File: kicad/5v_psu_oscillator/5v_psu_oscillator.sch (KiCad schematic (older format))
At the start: 30 parts, among them P1 IEC-C6, P2 CONN_01X03, SW1 DPST, T1 BV 030-7329.0 T, U1 LT1017, U2 74HC08, U3 LM2675N-5.0, U4 74HC4024

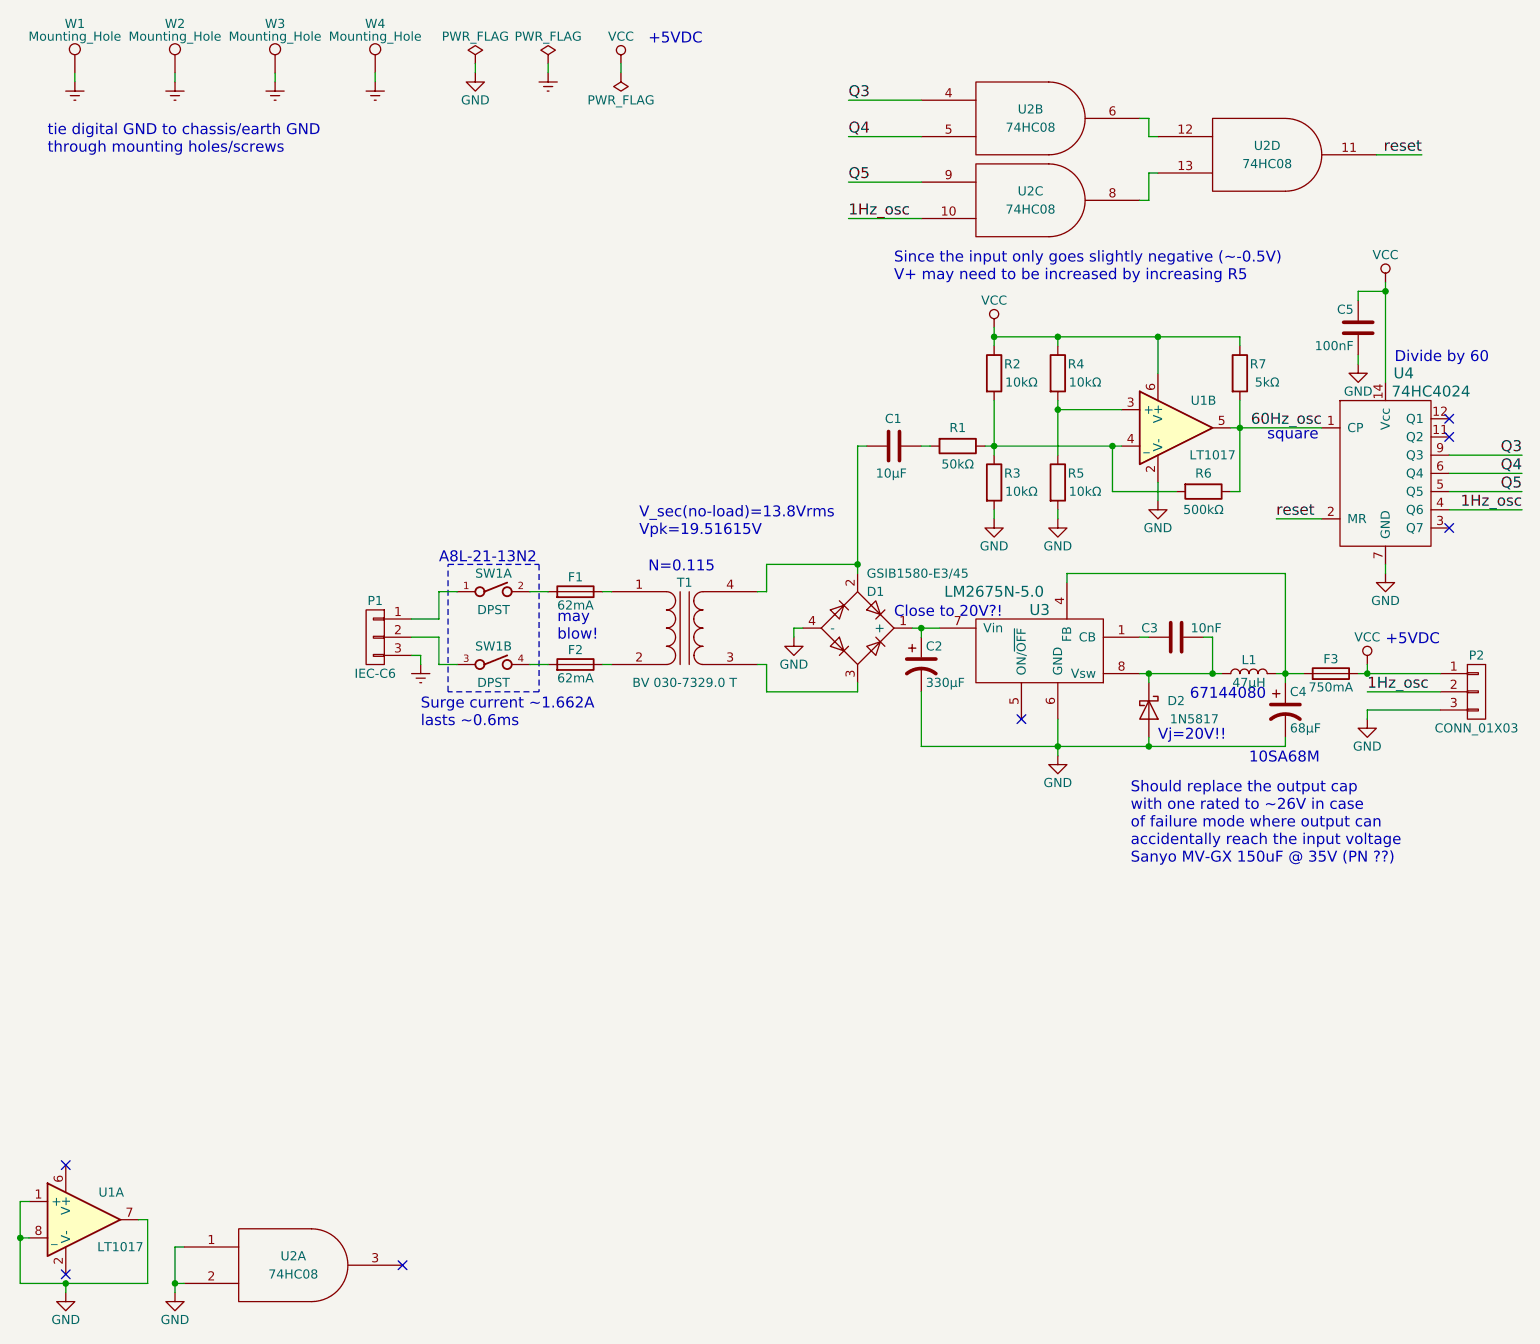
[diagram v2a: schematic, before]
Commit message: Add new 5V psu and oscillator simulation projects/data, include additional 100uFinput capacitor to the buck converter for less input ripple
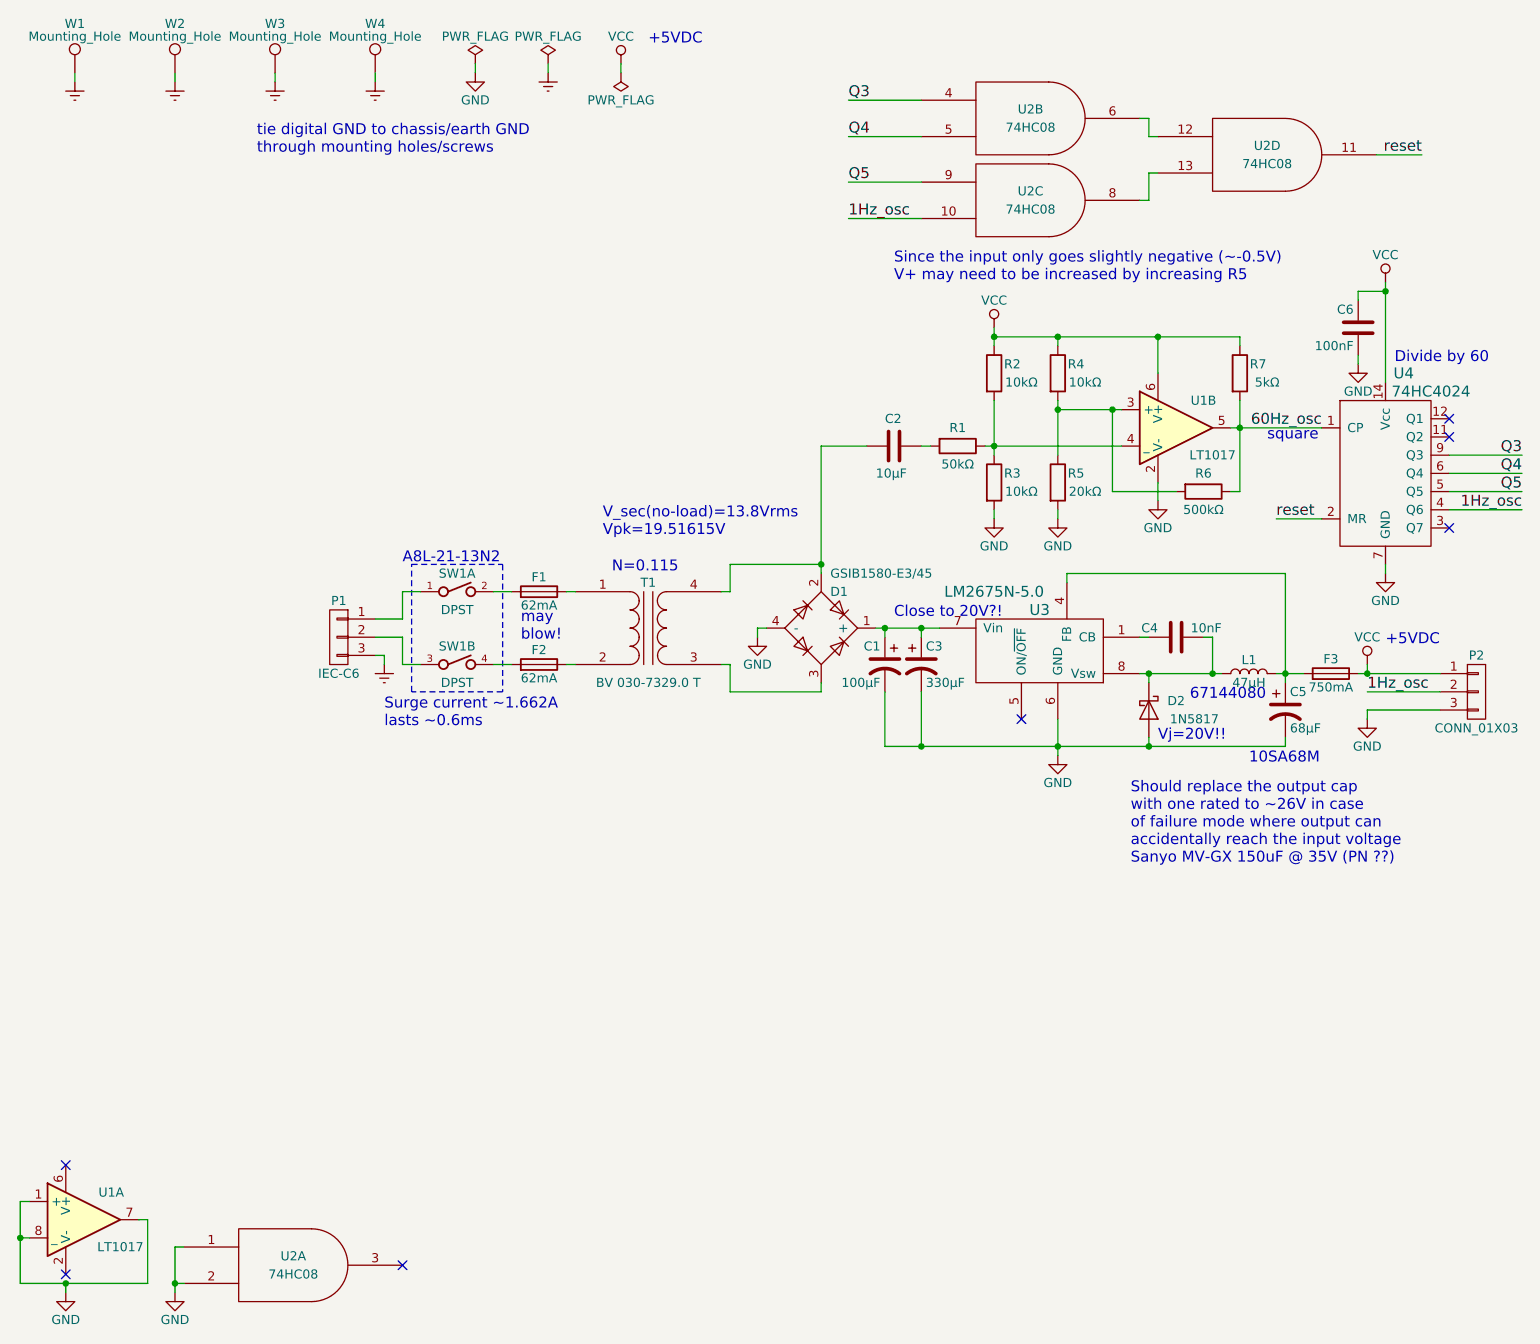
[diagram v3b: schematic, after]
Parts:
- added C1: 100μF, symbol CP1
- R5: value 10kΩ -> 20kΩ
- renumbered C1 to C2, C2 to C3, C3 to C4, C4 to C5, C5 to C6
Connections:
- net GND: now also C1.2
- net at C3.1, D1.1 (+), U3.7 (Vin): now also C1.1
- net at R1.1, R2.2, R3.1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: no longer R6.2
- net at R4.2, R5.1, U1.3 (+): now also R6.2
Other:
- moved on the sheet: D1, F1, F2, P1, SW1A, SW1B, T1
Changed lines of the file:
@@
 L Transformer_1P_1S T1
 U 1 1 59065B01
-P 4200 3900
-F 0 "T1" H 4200 4150 50  0000 C CNN
-F 1 "BV 030-7329.0 T" H 4200 3600 50  0000 C CNN
-F 2 "" H 4200 3900 50  0001 C CNN
-F 3 "" H 4200 3900 50  0000 C CNN
-	1    4200 3900
+P 4000 3900
+F 0 "T1" H 4000 4150 50  0000 C CNN
+F 1 "BV 030-7329.0 T" H 4000 3600 50  0000 C CNN
+F 2 "" H 4000 3900 50  0001 C CNN
+F 3 "" H 4000 3900 50  0000 C CNN
+	1    4000 3900
 	1    0    0    -1
 $EndComp
@@
 L Fuse F1
 U 1 1 59065C6E
-P 3600 3700
-F 0 "F1" V 3680 3700 50  0000 C CNN
-F 1 "62mA" V 3525 3700 50  0000 C CNN
-F 2 "Resistors_THT:R_Axial_DIN0309_L9.0mm_D3.2mm_P12.70mm_Horizontal" V 3530 3700 50  0001 C CNN
-F 3 "" H 3600 3700 50  0000 C CNN
-	1    3600 3700
+P 3400 3700
+F 0 "F1" V 3480 3700 50  0000 C CNN
+F 1 "62mA" V 3325 3700 50  0000 C CNN
+F 2 "Resistors_THT:R_Axial_DIN0309_L9.0mm_D3.2mm_P12.70mm_Horizontal" V 3330 3700 50  0001 C CNN
+F 3 "" H 3400 3700 50  0000 C CNN
+	1    3400 3700
 	0    1    -1   0
 $EndComp
@@
 L Fuse F2
 U 1 1 59065D5D
-P 3600 4100
-F 0 "F2" V 3680 4100 50  0000 C CNN
-F 1 "62mA" V 3525 4100 50  0000 C CNN
-F 2 "Resistors_THT:R_Axial_DIN0309_L9.0mm_D3.2mm_P12.70mm_Horizontal" V 3530 4100 50  0001 C CNN
-F 3 "" H 3600 4100 50  0000 C CNN
-	1    3600 4100
+P 3400 4100
+F 0 "F2" V 3480 4100 50  0000 C CNN
+F 1 "62mA" V 3325 4100 50  0000 C CNN
+F 2 "Resistors_THT:R_Axial_DIN0309_L9.0mm_D3.2mm_P12.70mm_Horizontal" V 3330 4100 50  0001 C CNN
+F 3 "" H 3400 4100 50  0000 C CNN
+	1    3400 4100
 	0    1    -1   0
 $EndComp
@@
 L D_Bridge_+AA- D1
 U 1 1 59065F83
-P 5150 3900
-F 0 "D1" H 5200 4100 50  0000 L CNN
-F 1 "GSIB1580-E3/45" H 5200 4200 50  0000 L CNN
-F 2 "" H 5150 3900 50  0001 C CNN
-F 3 "" H 5150 3900 50  0000 C CNN
-	1    5150 3900
+P 4950 3900
+F 0 "D1" H 5000 4100 50  0000 L CNN
+F 1 "GSIB1580-E3/45" H 5000 4200 50  0000 L CNN
+F 2 "" H 4950 3900 50  0001 C CNN
+F 3 "" H 4950 3900 50  0000 C CNN
+	1    4950 3900
 	1    0    0    -1
 $EndComp
@@
 L DPST SW1
 U 1 1 59066ED6
-P 3150 3700
-F 0 "SW1" H 3150 3800 50  0000 C CNN
-F 1 "DPST" H 3150 3600 50  0000 C CNN
-F 2 "" H 3150 3700 60  0001 C CNN
-F 3 "" H 3150 3700 60  0001 C CNN
-	1    3150 3700
+P 2950 3700
+F 0 "SW1" H 2950 3800 50  0000 C CNN
+F 1 "DPST" H 2950 3600 50  0000 C CNN
+F 2 "" H 2950 3700 60  0001 C CNN
+F 3 "" H 2950 3700 60  0001 C CNN
+	1    2950 3700
 	1    0    0    -1
 $EndComp
@@
 L DPST SW1
 U 2 1 59066F0F
-P 3150 4100
-F 0 "SW1" H 3150 4200 50  0000 C CNN
-F 1 "DPST" H 3150 4000 50  0000 C CNN
-F 2 "" H 3150 4100 60  0001 C CNN
-F 3 "" H 3150 4100 60  0001 C CNN
-	2    3150 4100
-	1    0    0    -1
-$EndComp
-$Comp
-L CP1 C2
+P 2950 4100
+F 0 "SW1" H 2950 4200 50  0000 C CNN
+F 1 "DPST" H 2950 4000 50  0000 C CNN
+F 2 "" H 2950 4100 60  0001 C CNN
+F 3 "" H 2950 4100 60  0001 C CNN
+	2    2950 4100
+	1    0    0    -1
+$EndComp
+$Comp
+L CP1 C3
 U 1 1 59067137
 P 5500 4100
-F 0 "C2" H 5525 4200 50  0000 L CNN
+F 0 "C3" H 5525 4200 50  0000 L CNN
 F 1 "330μF" H 5525 4000 50  0000 L CNN
 F 2 "Capacitors_THT:CP_Radial_D10.0mm_P5.00mm" H 5500 4100 50  0001 C CNN
@@
 	1    0    0    -1
 $EndComp
-Text Notes 3950 3400 0    60   ~ 0
+Text Notes 3750 3400 0    60   ~ 0
 V_sec(no-load)=13.8Vrms\nVpk=19.51615V
-Text Notes 4000 3600 0    60   ~ 0
+Text Notes 3800 3600 0    60   ~ 0
 N=0.115
 $Comp
@@
 $EndComp
 $Comp
-L C C3
+L C C4
 U 1 1 590696A4
 P 6900 3950
-F 0 "C3" V 6950 4050 50  0000 L CNN
+F 0 "C4" V 6950 4050 50  0000 L CNN
 F 1 "10nF" V 6950 3700 50  0000 L CNN
 F 2 "Capacitors_THT:C_Disc_D3.4mm_W2.1mm_P2.50mm" H 6938 3800 50  0001 C CNN
@@
 L CONN_01X03 P1
 U 1 1 5906AD4D
-P 2500 3950
-F 0 "P1" H 2500 4150 50  0000 C CNN
-F 1 "IEC-C6" H 2500 3750 50  0000 C CNN
-F 2 "" H 2500 3950 50  0001 C CNN
-F 3 "" H 2500 3950 50  0000 C CNN
-	1    2500 3950
+P 2300 3950
+F 0 "P1" H 2300 4150 50  0000 C CNN
+F 1 "IEC-C6" H 2300 3750 50  0000 C CNN
+F 2 "" H 2300 3950 50  0001 C CNN
+F 3 "" H 2300 3950 50  0000 C CNN
+	1    2300 3950
 	-1   0    0    -1
 $EndComp
@@
 $EndComp
 Wire Wire Line
-	4800 3950 4800 3900
-Wire Wire Line
-	4800 3900 4850 3900
-Wire Wire Line
-	4600 4100 4650 4100
-Wire Wire Line
-	4650 4100 4650 4250
-Wire Wire Line
-	5150 4250 5150 4200
-Wire Wire Line
-	4600 3700 4650 3700
-Wire Wire Line
-	4650 3700 4650 3550
-Wire Wire Line
-	4650 3550 5150 3550
-Wire Wire Line
-	5150 2900 5150 3600
-Wire Wire Line
-	3800 3700 3750 3700
-Wire Wire Line
-	3800 4100 3750 4100
-Wire Wire Line
-	3450 3700 3350 3700
-Wire Wire Line
-	3350 4100 3450 4100
-Wire Wire Line
-	2950 3700 2850 3700
-Wire Wire Line
-	2950 4100 2850 4100
+	4600 3950 4600 3900
+Wire Wire Line
+	4600 3900 4650 3900
+Wire Wire Line
+	4400 4100 4450 4100
+Wire Wire Line
+	4450 4100 4450 4250
+Wire Wire Line
+	4950 4250 4950 4200
+Wire Wire Line
+	4400 3700 4450 3700
+Wire Wire Line
+	4450 3700 4450 3550
+Wire Wire Line
+	4450 3550 4950 3550
+Wire Wire Line
+	4950 2900 4950 3600
+Wire Wire Line
+	3600 3700 3550 3700
+Wire Wire Line
+	3600 4100 3550 4100
+Wire Wire Line
+	3250 3700 3150 3700
+Wire Wire Line
+	3150 4100 3250 4100
+Wire Wire Line
+	2750 3700 2650 3700
+Wire Wire Line
+	2750 4100 2650 4100
 Wire Wire Line
 	5500 4550 5500 4250
 Wire Wire Line
-	5500 3950 5500 3900
-Wire Wire Line
-	5450 3900 5600 3900
+	5500 3900 5500 3950
+Wire Wire Line
+	5250 3900 5600 3900
 Connection ~ 5500 3900
 Wire Wire Line
 	6250 4400 6250 4600
 Wire Notes Line
-	2900 3550 3400 3550
+	2700 3550 3200 3550
 Wire Notes Line
-	3400 3550 3400 4250
+	3200 3550 3200 4250
 Wire Notes Line
-	3400 4250 2900 4250
+	3200 4250 2700 4250
 Wire Notes Line
-	2900 4250 2900 3550
+	2700 4250 2700 3550
 Wire Wire Line
 	6750 4550 6750 4500
@@
 	7950 4150 7950 4100
 Wire Wire Line
-	2750 4100 2750 4050
-Wire Wire Line
-	2750 4050 2700 4050
-Wire Wire Line
-	2700 3850 2850 3850
-Wire Wire Line
-	2850 3850 2850 3700
-Wire Wire Line
-	2700 3950 2850 3950
-Wire Wire Line
-	2850 3950 2850 4100
+	2550 4100 2550 4050
+Wire Wire Line
+	2550 4050 2500 4050
+Wire Wire Line
+	2500 3850 2650 3850
+Wire Wire Line
+	2650 3850 2650 3700
+Wire Wire Line
+	2500 3950 2650 3950
+Wire Wire Line
+	2650 3950 2650 4100
 Wire Wire Line
 	7950 4400 7950 4350
@@
 67144080
 $Comp
-L CP1 C4
+L CP1 C5
 U 1 1 59076BE1
 P 7500 4350
-F 0 "C4" H 7525 4450 50  0000 L CNN
+F 0 "C5" H 7525 4450 50  0000 L CNN
 F 1 "68μF" H 7525 4250 50  0000 L CNN
 F 2 "Capacitors_THT:CP_Radial_D6.3mm_P2.50mm" H 7500 4350 50  0001 C CNN
@@
 	1    0    0    -1
 $EndComp
-Text Notes 2850 3550 0    60   ~ 0
+Text Notes 2650 3550 0    60   ~ 0
 A8L-21-13N2
 NoConn ~ 6050 4400
-Text Notes 2750 4450 0    60   ~ 0
+Text Notes 2550 4450 0    60   ~ 0
 Surge current ~~1.662A\nlasts ~~0.6ms
 $Bitmap
@@
 Text Notes 5350 3850 0    60   ~ 0
 Close to 20V?!
-Text Notes 3500 3975 0    60   ~ 0
+Text Notes 3300 3975 0    60   ~ 0
 may\nblow!
 $Comp
@@
 P 6250 3100
 F 0 "R5" H 6350 3150 50  0000 C CNN
-F 1 "10kΩ" H 6400 3050 50  0000 C CNN
+F 1 "20kΩ" H 6400 3050 50  0000 C CNN
 F 2 "Resistors_THT:R_Axial_DIN0207_L6.3mm_D2.5mm_P7.62mm_Horizontal" V 6180 3100 50  0001 C CNN
 F 3 "" H 6250 3100 50  0000 C CNN
@@
 	6250 2650 6250 2950
 Wire Wire Line
-	6600 2700 6250 2700
+	6250 2700 6600 2700
 Connection ~ 6250 2700
 Connection ~ 5900 2900
@@
 $EndComp
 $Comp
-L C C1
+L C C2
 U 1 1 5908DC57
 P 5350 2900
-F 0 "C1" V 5200 2850 50  0000 L CNN
+F 0 "C2" V 5200 2850 50  0000 L CNN
 F 1 "10μF" V 5500 2800 50  0000 L CNN
 F 2 "Capacitors_THT:C_Disc_D5.0mm_W2.5mm_P2.50mm" H 5388 2750 50  0001 C CNN
@@
 	6900 3150 6550 3150
 Wire Wire Line
-	6550 3150 6550 2900
-Connection ~ 6550 2900
-Wire Wire Line
 	7250 3150 7200 3150
 Wire Wire Line
-	5150 2900 5200 2900
-Connection ~ 5150 3550
+	4950 2900 5200 2900
+Connection ~ 4950 3550
 Text Notes 7400 2875 0    60   ~ 0
 square
@@
 	5100 1650 5500 1650
 $Comp
-L C C5
+L C C6
 U 1 1 590A5FBC
 P 7900 2250
-F 0 "C5" H 7925 2350 50  0000 L CNN
+F 0 "C6" H 7925 2350 50  0000 L CNN
 F 1 "100nF" H 7925 2150 50  0000 L CNN
 F 2 "Capacitors_THT:C_Disc_D3.8mm_W2.6mm_P2.50mm" H 7938 2100 50  0001 C CNN
@@
 	6800 3100 6800 3200
 Wire Wire Line
-	4650 4250 5150 4250
-Wire Wire Line
-	5500 4550 7500 4550
+	4450 4250 4950 4250
+Wire Wire Line
+	5300 4550 7500 4550
 $Comp
 L GND #PWR01
 U 1 1 590B43E1
-P 4800 3950
-F 0 "#PWR01" H 4800 3700 50  0001 C CNN
-F 1 "GND" H 4800 3800 50  0000 C CNN
-F 2 "" H 4800 3950 50  0000 C CNN
-F 3 "" H 4800 3950 50  0000 C CNN
-	1    4800 3950
+P 4600 3950
+F 0 "#PWR01" H 4600 3700 50  0001 C CNN
+F 1 "GND" H 4600 3800 50  0000 C CNN
+F 2 "" H 4600 3950 50  0000 C CNN
+F 3 "" H 4600 3950 50  0000 C CNN
+	1    4600 3950
 	1    0    0    -1
 $EndComp
@@
 $EndComp
 NoConn ~ 800  6850
-Text Notes 700  1300 0    60   ~ 0
+Text Notes 1850 1300 0    60   ~ 0
 tie digital GND to chassis/earth GND\nthrough mounting holes/screws
 $Comp
@@
 L Earth #PWR018
 U 1 1 59DF4591
-P 2750 4100
-F 0 "#PWR018" H 2750 3850 50  0001 C CNN
-F 1 "Earth" H 2750 3950 50  0001 C CNN
-F 2 "" H 2750 4100 50  0001 C CNN
-F 3 "" H 2750 4100 50  0001 C CNN
-	1    2750 4100
+P 2550 4100
+F 0 "#PWR018" H 2550 3850 50  0001 C CNN
+F 1 "Earth" H 2550 3950 50  0001 C CNN
+F 2 "" H 2550 4100 50  0001 C CNN
+F 3 "" H 2550 4100 50  0001 C CNN
+	1    2550 4100
 	1    0    0    -1
 $EndComp
@@
 Text Notes 6650 5200 0    60   ~ 0
 Should replace the output cap\nwith one rated to ~~26V in case\nof failure mode where output can\naccidentally reach the input voltage\nSanyo MV-GX 150uF @ 35V (PN ??)
+Wire Wire Line
+	6550 3150 6550 2700
+Connection ~ 6550 2700
+$Comp
+L CP1 C1
+U 1 1 59E9ADF5
+P 5300 4100
+F 0 "C1" H 5325 4200 50  0000 L CNN
+F 1 "100μF" H 5325 4000 50  0000 L CNN
+F 2 "" H 5300 4100 50  0001 C CNN
+F 3 "" H 5300 4100 50  0001 C CNN
+	1    5300 4100
+	-1   0    0    -1
+$EndComp
+Wire Wire Line
+	5300 3950 5300 3900
+Connection ~ 5300 3900
+Wire Wire Line
+	5300 4250 5300 4550
+Connection ~ 5500 4550
 $EndSCHEMATC
